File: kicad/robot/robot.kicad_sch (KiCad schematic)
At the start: 54 parts, among them U1 DNP, U7 AP2502KTR-G1

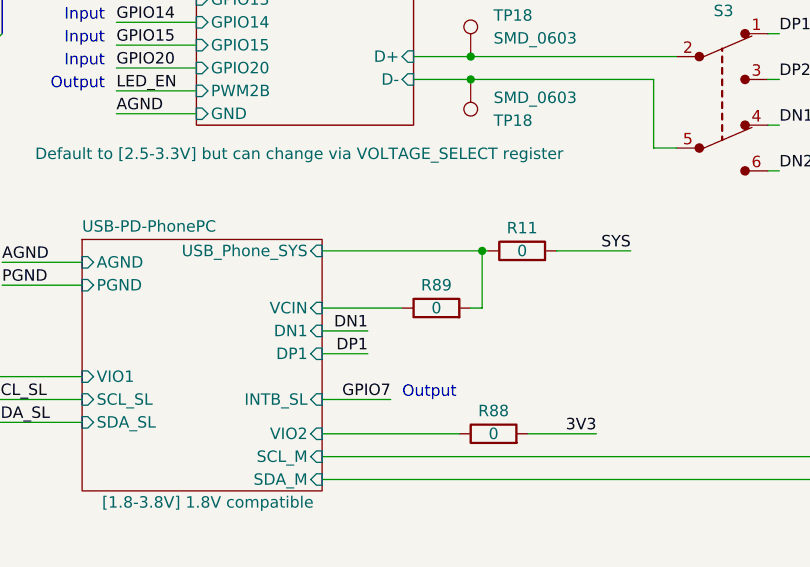
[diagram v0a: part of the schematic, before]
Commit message: Major revision moving motor drivers closer to motor headers
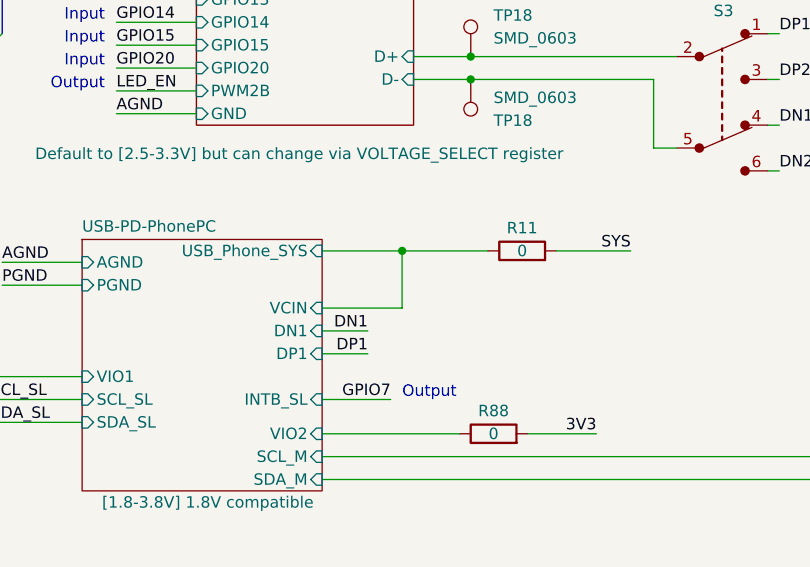
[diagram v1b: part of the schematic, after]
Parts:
- removed R89: 0, robot:R_0603_1608Metric, symbol Device:R
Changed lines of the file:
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@@
   (junction (at 140.97 187.325) (diameter 0) (color 0 0 0 0)
   )
-  (junction (at 180.34 144.78) (diameter 0) (color 0 0 0 0)
-  )
   (junction (at 127 76.2) (diameter 0) (color 0 0 0 0)
   )
@@
   )
   (junction (at 179.07 123.19) (diameter 0) (color 0 0 0 0)
+  )
+  (junction (at 171.45 144.78) (diameter 0) (color 0 0 0 0)
   )
   (junction (at 175.895 93.98) (diameter 0) (color 0 0 0 0)
@@
     (stroke (width 0) (type default))
   )
-  (wire (pts (xy 162.56 144.78) (xy 180.34 144.78))
-    (stroke (width 0) (type default))
-  )
   (bus (pts (xy 206.375 63.5) (xy 206.375 66.04))
     (stroke (width 0) (type default) (color 194 0 194 1))
@@
     (stroke (width 0) (type default))
   )
+  (wire (pts (xy 171.45 144.78) (xy 180.975 144.78))
+    (stroke (width 0) (type default))
+  )
   (wire (pts (xy 41.91 20.32) (xy 55.88 20.32))
     (stroke (width 0) (type default))
@@
     (stroke (width 0) (type default) (color 255 0 6 1))
   )
-  (wire (pts (xy 180.34 144.78) (xy 180.34 151.13))
-    (stroke (width 0) (type default))
-  )
   (wire (pts (xy 229.87 78.74) (xy 219.71 78.74))
     (stroke (width 0) (type default))
@@
     (stroke (width 0) (type default))
   )
+  (wire (pts (xy 171.45 144.78) (xy 171.45 151.13))
+    (stroke (width 0) (type default))
+  )
   (wire (pts (xy 185.42 39.37) (xy 191.77 39.37))
     (stroke (width 0) (type default))
@@
   )
   (wire (pts (xy 220.98 93.98) (xy 229.87 93.98))
-    (stroke (width 0) (type default))
-  )
-  (wire (pts (xy 180.34 151.13) (xy 179.07 151.13))
     (stroke (width 0) (type default))
   )
@@
     (stroke (width 0) (type default))
   )
-  (wire (pts (xy 180.34 144.78) (xy 180.975 144.78))
+  (wire (pts (xy 162.56 144.78) (xy 171.45 144.78))
     (stroke (width 0) (type default))
   )
@@
         )
       )
-    )
-  )
-  (symbol (lib_id "Device:R") (at 175.26 151.13 90) (unit 1)
-    (in_bom yes) (on_board yes) (dnp no)
-    (property "Reference" "R89" (at 175.26 148.59 90)
-      (effects (font (size 1.27 1.27)))
-    )
-    (property "Value" "0" (at 175.26 151.13 90)
-      (effects (font (size 1.27 1.27)))
-    )
-    (property "Footprint" "robot:R_0603_1608Metric" (at 175.26 152.908 90)
-      (effects (font (size 1.27 1.27)) hide)
-    )
-    (property "Datasheet" "~" (at 175.26 151.13 0)
-      (effects (font (size 1.27 1.27)) hide)
-    )
-    (property "Manufacturer" "Stackpole Electronics" (at 175.26 151.13 90)
-      (effects (font (size 1.27 1.27)) hide)
-    )
-    (property "Part Number" "RMCF0603ZT0R00" (at 175.26 151.13 90)
-      (effects (font (size 1.27 1.27)) hide)
-    )
-    (property "Stock" "" (at 175.26 151.13 0)
-      (effects (font (size 1.27 1.27)) hide)
-    )
-    (pin "1")
-    (pin "2")
-    (instances
-      (project "robot"
-        (path "/0c7b298e-2d07-4b1f-b033-e95f02d45089"
-          (reference "R89") (unit 1)
-        )
-      )

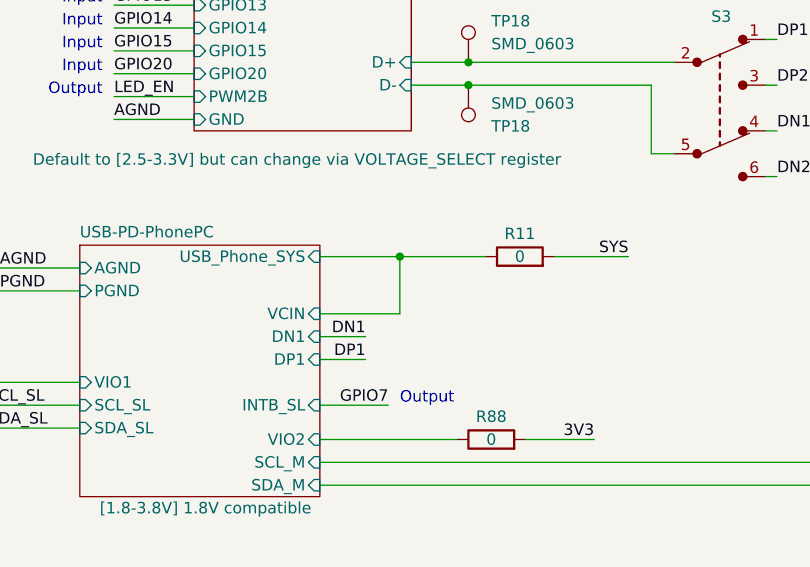
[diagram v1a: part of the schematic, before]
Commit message: Fixing Vcin net tie issue
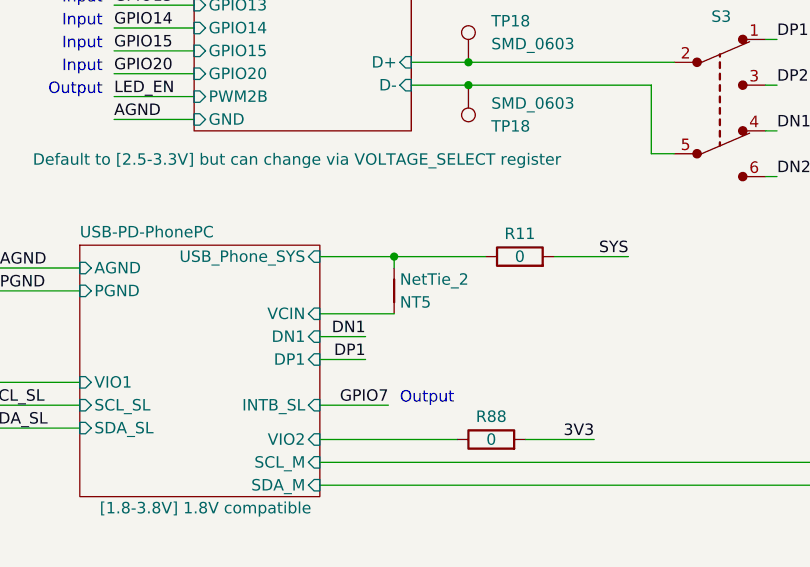
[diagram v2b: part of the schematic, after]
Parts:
- added NT5: NetTie_2, robot:NetTie-_SMD_Pad6mil, symbol Device:NetTie_2
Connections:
- net USB-PD-PhonePC/USB_Phone_SYS: now also NT5.2
- new net USB-PD-PhonePC/VCIN: NT5.1
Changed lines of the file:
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@@
   (junction (at 179.07 123.19) (diameter 0) (color 0 0 0 0)
   )
-  (junction (at 171.45 144.78) (diameter 0) (color 0 0 0 0)
-  )
   (junction (at 175.895 93.98) (diameter 0) (color 0 0 0 0)
   )
@@
   (junction (at 259.715 69.85) (diameter 0) (color 0 0 0 0)
   )
+  (junction (at 170.815 144.78) (diameter 0) (color 0 0 0 0)
+  )
   (junction (at 261.62 83.82) (diameter 0) (color 0 0 0 0)
   )
@@
     (stroke (width 0) (type default))
   )
+  (wire (pts (xy 170.815 144.78) (xy 180.975 144.78))
+    (stroke (width 0) (type default))
+  )
   (bus (pts (xy 206.375 63.5) (xy 206.375 66.04))
     (stroke (width 0) (type default) (color 194 0 194 1))
@@
     (stroke (width 0) (type default))
   )
-  (wire (pts (xy 162.56 151.13) (xy 171.45 151.13))
-    (stroke (width 0) (type default))
-  )
   (wire (pts (xy 63.5 20.32) (xy 63.5 21.59))
     (stroke (width 0) (type default))
@@
     (stroke (width 0) (type default))
   )
-  (wire (pts (xy 171.45 144.78) (xy 180.975 144.78))
-    (stroke (width 0) (type default))
-  )
   (wire (pts (xy 41.91 20.32) (xy 55.88 20.32))
     (stroke (width 0) (type default))
@@
     (stroke (width 0) (type default))
   )
-  (wire (pts (xy 171.45 144.78) (xy 171.45 151.13))
-    (stroke (width 0) (type default))
-  )
   (wire (pts (xy 185.42 39.37) (xy 191.77 39.37))
     (stroke (width 0) (type default))
@@
     (stroke (width 0) (type default))
   )
-  (wire (pts (xy 162.56 144.78) (xy 171.45 144.78))
-    (stroke (width 0) (type default))
-  )
   (wire (pts (xy 116.205 123.19) (xy 124.46 123.19))
     (stroke (width 0) (type default))
@@
     (stroke (width 0) (type default))
   )
+  (wire (pts (xy 170.815 144.78) (xy 170.815 146.05))
+    (stroke (width 0) (type default))
+  )
   (wire (pts (xy 259.715 76.2) (xy 255.27 76.2))
     (stroke (width 0) (type default))
@@
     (stroke (width 0) (type default))
   )
+  (wire (pts (xy 162.56 144.78) (xy 170.815 144.78))
+    (stroke (width 0) (type default))
+  )
   (wire (pts (xy 138.43 195.58) (xy 149.225 195.58))
     (stroke (width 0) (type default))
@@
     (stroke (width 0) (type default))
   )
+  (wire (pts (xy 162.56 151.13) (xy 170.815 151.13))
+    (stroke (width 0) (type default))
+  )
   (wire (pts (xy 36.195 50.165) (xy 45.085 50.165))
     (stroke (width 0) (type default))
@@
         )
       )
+    )
+  )
+  (symbol (lib_id "Device:NetTie_2") (at 170.815 148.59 270) (mirror x) (unit 1)
+    (in_bom no) (on_board yes) (dnp no)
+    (property "Reference" "NT5" (at 171.45 149.86 90)
+      (effects (font (size 1.27 1.27)) (justify left))
+    )
+    (property "Value" "NetTie_2" (at 171.45 147.32 90)
+      (effects (font (size 1.27 1.27)) (justify left))
+    )
+    (property "Footprint" "robot:NetTie-_SMD_Pad6mil" (at 170.815 148.59 0)
+      (effects (font (size 1.27 1.27)) hide)
+    )
+    (property "Datasheet" "~" (at 170.815 148.59 0)
+      (effects (font (size 1.27 1.27)) hide)
+    )
+    (property "Manufacturer" "N/A" (at 170.815 148.59 0)
+      (effects (font (size 1.27 1.27)) hide)
+    )
+    (property "Part Number" "N/A" (at 170.815 148.59 0)
+      (effects (font (size 1.27 1.27)) hide)
+    )
+    (property "Stock" "" (at 170.815 148.59 0)
+      (effects (font (size 1.27 1.27)) hide)
+    )
+    (pin "1")
+    (pin "2")
+    (instances
+      (project "robot"
+        (path "/0c7b298e-2d07-4b1f-b033-e95f02d45089/3fab603d-ed65-41bd-8de1-51639e39cb06"
+          (reference "NT5") (unit 1)
+        )
+        (path "/0c7b298e-2d07-4b1f-b033-e95f02d45089/aaf20b87-68dc-43c9-a7d3-4ceda8b87424"
+          (reference "NT15") (unit 1)
+        )
+        (path "/0c7b298e-2d07-4b1f-b033-e95f02d45089/427922e5-a943-4728-8788-709c0c3b2395"
+          (reference "NT16") (unit 1)
+        )
+        (path "/0c7b298e-2d07-4b1f-b033-e95f02d45089"
+          (reference "NT18") (unit 1)
+        )
+        (path "/0c7b298e-2d07-4b1f-b033-e95f02d45089/b1182274-8387-45c9-b9a4-abcd767ed6f2"
+          (reference "NT18") (unit 1)
+        )
+      )

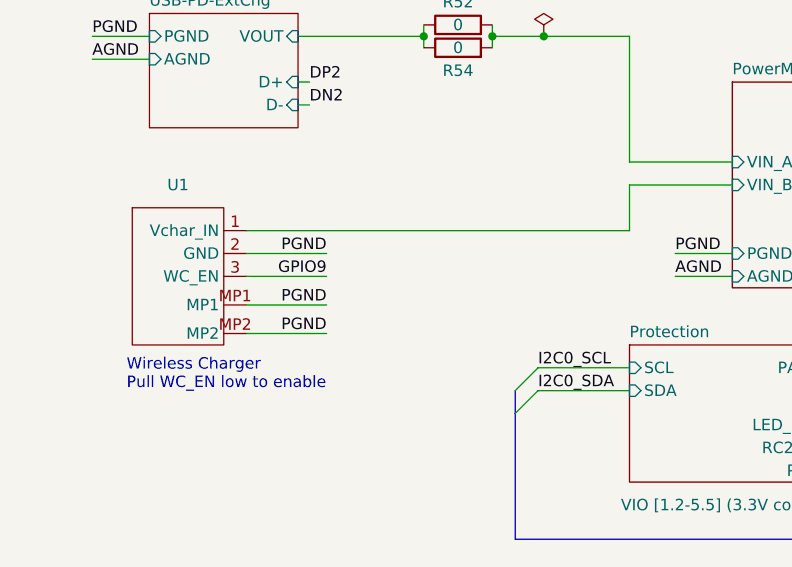
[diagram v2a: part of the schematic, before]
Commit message: Added wireless recevier separate from header
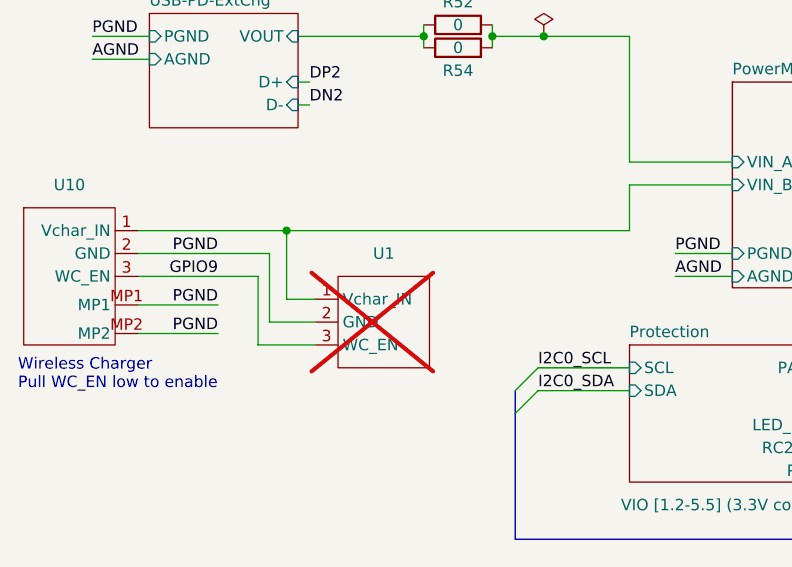
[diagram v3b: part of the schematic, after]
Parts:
- added U10: BM03BPASS1TFTLFSN, robot:BM03BPASS1TFTLFSN, symbol robot:BM03BPASS1TFTLFSN
- U1: footprint robot:BM03BPASS1TFTLFSN -> (none); now not fitted
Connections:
- net AGND: now also U10.2 (GND), U10.MP1, U10.MP2; no longer U1.MP1, U1.MP2
- net GPIO9: now also U10.3 (WC_EN)
- net PowerMux/VIN_B: now also U10.1 (Vchar_IN)
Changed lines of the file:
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@@
   (junction (at 127 76.2) (diameter 0) (color 0 0 0 0)
+  )
+  (junction (at 40.64 41.91) (diameter 0) (color 0 0 0 0)
   )
   (junction (at 178.435 96.52) (diameter 0) (color 0 0 0 0)
@@
     (stroke (width 0) (type default))
   )
-  (wire (pts (xy 36.195 41.91) (xy 78.74 41.91))
-    (stroke (width 0) (type default))
-  )
-  (wire (pts (xy 45.085 46.99) (xy 36.195 46.99))
+  (wire (pts (xy 24.13 41.91) (xy 40.64 41.91))
+    (stroke (width 0) (type default))
+  )
+  (wire (pts (xy 24.13 46.99) (xy 37.465 46.99))
     (stroke (width 0) (type default))
   )
@@
     (stroke (width 0) (type default))
   )
+  (wire (pts (xy 38.735 44.45) (xy 38.735 52.07))
+    (stroke (width 0) (type default))
+  )
   (wire (pts (xy 107.315 106.68) (xy 107.315 113.03))
     (stroke (width 0) (type default))
@@
     (stroke (width 0) (type default))
   )
+  (wire (pts (xy 37.465 46.99) (xy 37.465 54.61))
+    (stroke (width 0) (type default))
+  )
   (wire (pts (xy 271.145 72.39) (xy 278.765 72.39))
     (stroke (width 0) (type default))
@@
     (stroke (width 0) (type default) (color 194 0 194 1))
   )
-  (wire (pts (xy 36.195 53.34) (xy 45.085 53.34))
+  (wire (pts (xy 24.13 53.34) (xy 33.02 53.34))
     (stroke (width 0) (type default))
   )
   (wire (pts (xy 139.7 106.68) (xy 148.59 106.68))
+    (stroke (width 0) (type default))
+  )
+  (wire (pts (xy 40.64 41.91) (xy 78.74 41.91))
     (stroke (width 0) (type default))
   )
@@
     (stroke (width 0) (type default))
   )
-  (wire (pts (xy 36.195 44.45) (xy 45.085 44.45))
+  (wire (pts (xy 24.13 44.45) (xy 38.735 44.45))
     (stroke (width 0) (type default))
   )
@@
     (stroke (width 0) (type default))
   )
+  (wire (pts (xy 38.735 52.07) (xy 43.815 52.07))
+    (stroke (width 0) (type default))
+  )
   (wire (pts (xy 213.36 130.81) (xy 212.09 130.81))
+    (stroke (width 0) (type default))
+  )
+  (wire (pts (xy 40.64 49.53) (xy 40.64 41.91))
     (stroke (width 0) (type default))
   )
@@
     (stroke (width 0) (type default))
   )
+  (wire (pts (xy 43.815 49.53) (xy 40.64 49.53))
+    (stroke (width 0) (type default))
+  )
   (wire (pts (xy 127 146.05) (xy 135.89 146.05))
     (stroke (width 0) (type default))
@@
     (stroke (width 0) (type default))
   )
+  (wire (pts (xy 37.465 54.61) (xy 43.815 54.61))
+    (stroke (width 0) (type default))
+  )
   (wire (pts (xy 162.56 144.78) (xy 170.815 144.78))
     (stroke (width 0) (type default))
@@
     (stroke (width 0) (type default))
   )
-  (wire (pts (xy 36.195 50.165) (xy 45.085 50.165))
+  (wire (pts (xy 24.13 50.165) (xy 33.02 50.165))
     (stroke (width 0) (type default))
   )
@@
     (effects (font (size 1.27 1.27)) (justify right bottom))
   )
-  (text "Wireless Charger\nPull WC_EN low to enable" (at 22.86 59.69 0)
+  (text "Wireless Charger\nPull WC_EN low to enable" (at 10.795 59.69 0)
     (effects (font (size 1.27 1.27)) (justify left bottom))
   )
@@
     (effects (font (size 1.27 1.27)) (justify left bottom))
   )
-  (label "GPIO9" (at 45.085 46.99 180) (fields_autoplaced)
+  (label "GPIO9" (at 33.02 46.99 180) (fields_autoplaced)
     (effects (font (size 1.27 1.27)) (justify right bottom))
   )
@@
     (effects (font (size 1.27 1.27)) (justify left bottom))
   )
-  (label "PGND" (at 45.085 53.34 180) (fields_autoplaced)
+  (label "PGND" (at 33.02 53.34 180) (fields_autoplaced)
     (effects (font (size 1.27 1.27)) (justify right bottom))
   )
@@
     (effects (font (size 1.27 1.27)) (justify left bottom))
   )
-  (label "PGND" (at 45.085 44.45 180) (fields_autoplaced)
-    (effects (font (size 1.27 1.27)) (justify right bottom))
-  )
-  (label "PGND" (at 45.085 50.165 180) (fields_autoplaced)
+  (label "PGND" (at 33.02 44.45 180) (fields_autoplaced)
+    (effects (font (size 1.27 1.27)) (justify right bottom))
+  )
+  (label "PGND" (at 33.02 50.165 180) (fields_autoplaced)
     (effects (font (size 1.27 1.27)) (justify right bottom))
   )
@@
     )
   )
-  (symbol (lib_id "robot:WRM483265-10F5-12V-G") (at 28.575 44.45 0) (unit 1)
-    (in_bom yes) (on_board yes) (dnp no)
-    (property "Reference" "U1" (at 28.575 36.83 0)
+  (symbol (lib_id "robot:WRM483265-10F5-12V-G") (at 51.435 52.07 0) (mirror y) (unit 1)
+    (in_bom yes) (on_board no) (dnp yes)
+    (property "Reference" "U1" (at 51.435 44.45 0)
       (effects (font (size 1.27 1.27)))
     )
-    (property "Value" "DNP" (at 28.575 36.83 0)
-      (effects (font (size 1.27 1.27)) hide)
-    )
-    (property "Footprint" "robot:BM03BPASS1TFTLFSN" (at 28.575 36.83 0)
-      (effects (font (size 1.27 1.27)) hide)
-    )
-    (property "Datasheet" "https://www.renesas.com/us/en/document/dst/p9221-r3-datasheet?language=en&r=394816" (at 28.575 36.83 0)
-      (effects (font (size 1.27 1.27)) hide)
-    )
-    (property "Part Number" "WRM483265-10F5-12V-G" (at 28.575 44.45 0)
-      (effects (font (size 1.27 1.27)) hide)
-    )
-    (property "Description" "Premade Wireless Rx Module (Seperate board, this represents just the connector pins)." (at 28.575 44.45 0)
-      (effects (font (size 1.27 1.27)) hide)
-    )
-    (property "Manufacturer" "TDK" (at 28.575 44.45 0)
-      (effects (font (size 1.27 1.27)) hide)
-    )
-    (property "Stock" "" (at 28.575 44.45 0)
+    (property "Value" "DNP" (at 51.435 44.45 0)
+      (effects (font (size 1.27 1.27)) hide)
+    )
+    (property "Footprint" "" (at 51.435 44.45 0)
+      (effects (font (size 1.27 1.27)) hide)
+    )
+    (property "Datasheet" "https://www.renesas.com/us/en/document/dst/p9221-r3-datasheet?language=en&r=394816" (at 51.435 44.45 0)
+      (effects (font (size 1.27 1.27)) hide)
+    )
+    (property "Part Number" "WRM483265-10F5-12V-G" (at 51.435 52.07 0)
+      (effects (font (size 1.27 1.27)) hide)
+    )
+    (property "Description" "Premade Wireless Rx Module (Seperate board, this represents just the connector pins)." (at 51.435 52.07 0)
+      (effects (font (size 1.27 1.27)) hide)
+    )
+    (property "Manufacturer" "TDK" (at 51.435 52.07 0)
+      (effects (font (size 1.27 1.27)) hide)
+    )
+    (property "Stock" "" (at 51.435 52.07 0)
       (effects (font (size 1.27 1.27)) hide)
     )
@@
     (pin "2")
     (pin "3")
-    (pin "MP1")
-    (pin "MP2")
     (instances
       (project "robot"
@@
         )
       )
+    )
+  )
+  (symbol (lib_id "robot:BM03BPASS1TFTLFSN") (at 16.51 44.45 0) (unit 1)
+    (in_bom yes) (on_board yes) (dnp no) (fields_autoplaced)
+    (property "Reference" "U10" (at 16.51 36.83 0)
+      (effects (font (size 1.27 1.27)))
+    )
+    (property "Value" "BM03BPASS1TFTLFSN" (at 16.51 36.83 0)
+      (effects (font (size 1.27 1.27)) hide)
+    )
+    (property "Footprint" "robot:BM03BPASS1TFTLFSN" (at 16.51 36.83 0)
+      (effects (font (size 1.27 1.27)) hide)
+    )
+    (property "Datasheet" "https://www.jst-mfg.com/product/pdf/eng/ePA-F.pdf" (at 16.51 36.83 0)
+      (effects (font (size 1.27 1.27)) hide)
+    )
+    (property "Part Number" "BM03B-PASS-1-TFT" (at 16.51 44.45 0)
+      (effects (font (size 1.27 1.27)) hide)
+    )
+    (property "Description" "3 pin header" (at 16.51 44.45 0)
+      (effects (font (size 1.27 1.27)) hide)
+    )
+    (property "Manufacturer" "JST" (at 16.51 44.45 0)
+      (effects (font (size 1.27 1.27)) hide)
+    )
+    (pin "1")
+    (pin "2")
+    (pin "3")
+    (pin "MP1")
+    (pin "MP2")
+    (instances
+      (project "robot"
+        (path "/0c7b298e-2d07-4b1f-b033-e95f02d45089"
+          (reference "U10") (unit 1)
+        )
+      )
